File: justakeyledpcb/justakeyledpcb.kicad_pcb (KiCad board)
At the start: 2 copper layers, 84.3 x 43 mm, 16 parts, among them SW1 SW_Push, SW2 SW_Push, SW3 SW_Push, SW4 SW_Push, U1 XIAO-RP2040-DIP

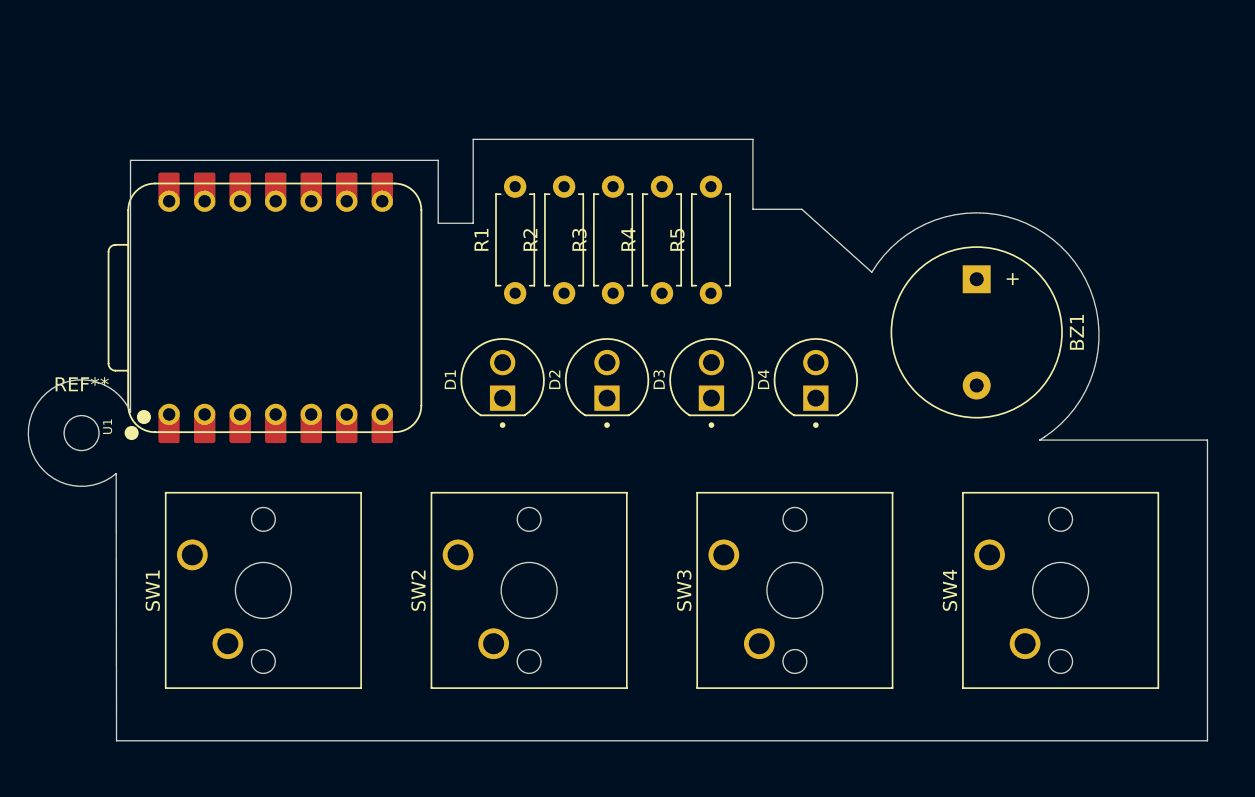
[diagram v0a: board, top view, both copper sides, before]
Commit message: Added the LED's footprints properly
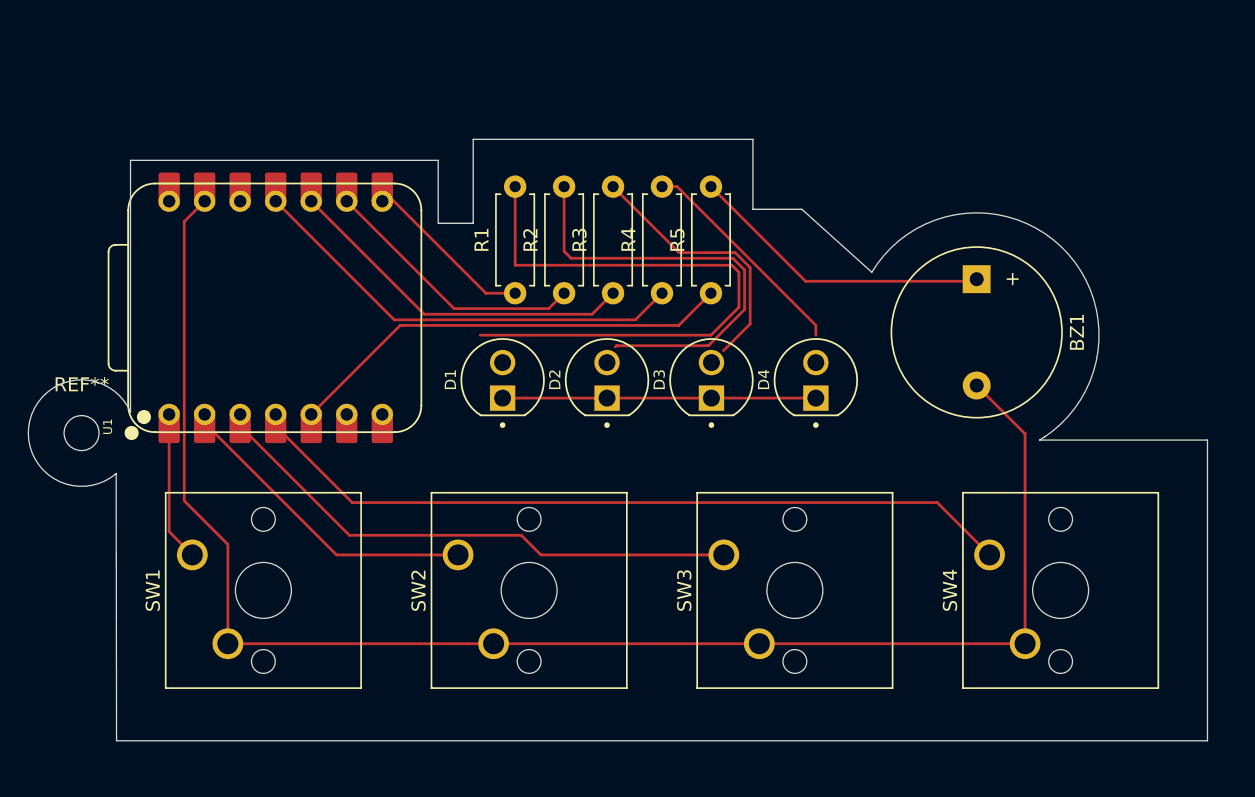
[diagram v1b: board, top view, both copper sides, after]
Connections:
- U1 pad 10: LED 1 -> LED 3
- U1 pad 11: LED 1 -> LED 4
- U1 pad 9: LED 1 -> LED 2
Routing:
- net GND: track 0.00 -> 110.4 mm
- net Button 4: track 0.00 -> 54.9 mm
- net Net-(D1-A): track 0.00 -> 43.7 mm
- net Button 3: track 0.00 -> 38.4 mm
- net Buzzer: track 0.00 -> 33.2 mm
- net LED 4: track 0.00 -> 31.9 mm
- net Net-(D2-A): track 0.00 -> 31.3 mm
- net LED 3: track 0.00 -> 25.5 mm
- net Button 2: track 0.00 -> 22.6 mm
- net (no net): track 0.00 -> 22.4 mm
- net Net-(BZ1-+): track 0.00 -> 21.9 mm
- net LED 2: track 0.00 -> 19.2 mm
- net Net-(D3-A): track 0.00 -> 18.9 mm
- net Net-(D4-A): track 0.00 -> 15.8 mm
- net LED 1: track 0.00 -> 12.6 mm
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
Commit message: FInalised the PCB Schematics and PCB Layout
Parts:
- D1, D2, D3, D4: value LED -> L08R5000Q1; footprint footprints:LEDRD254W57D500H1070 -> e390cee6c564169ed6d49fe7a268946ec8897500_l08r5000q1:LEDRD254W57D500H1070
- moved D1 23.4 mm to (150.5, 58.2)
- moved D4 21.5 mm to (128.0, 58.2)
- moved R1 15.1 mm to (143.0, 49.1)
- moved R5 15.1 mm to (127.0, 49.1)
- moved D2 8.49 mm to (143.0, 58.2)
- moved D3 6.61 mm to (135.5, 58.2)
- moved R4 1.95 mm to (139.0, 49.1)
- moved R3 1.88 mm to (135.0, 49.1)
- moved R2 1.76 mm to (131.0, 49.3)
- moved SW1 0.75 mm to (104.9, 70.5)
- moved SW2 0.75 mm to (123.9, 70.5)
- moved SW3 0.75 mm to (142.9, 70.5)
- moved SW4 0.75 mm to (161.9, 70.5)
- moved BZ1 0.50 mm to (161.5, 50.0)
- moved U1 0.43 mm to (110.9, 51.6)
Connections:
- D1 pad A: (no net) -> Net-(D1-PadA)
- D1 pad C: (no net) -> GND
- D2 pad A: (no net) -> Net-(D2-PadA)
- D2 pad C: (no net) -> GND
- D3 pad A: (no net) -> Net-(D3-PadA)
- D3 pad C: (no net) -> GND
- D4 pad A: (no net) -> Net-(D4-PadA)
- D4 pad C: (no net) -> GND
- R1 pad 1: LED 1 -> Buzzer
- R1 pad 2: Net-(D1-A) -> Net-(BZ1-+)
- R2 pad 2: Net-(D2-A) -> Net-(D3-PadA)
- R3 pad 2: Net-(D3-A) -> Net-(D2-PadA)
- R4 pad 2: Net-(D4-A) -> Net-(D1-PadA)
- R5 pad 1: Buzzer -> LED 1
- R5 pad 2: Net-(BZ1-+) -> Net-(D4-PadA)
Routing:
- net GND: track 110.4 -> 168.5 mm
- net Net-(D1-A): track 43.7 -> 0.00 mm
- net Net-(D4-PadA): track 0.00 -> 35.8 mm
- net Net-(D2-A): track 31.3 -> 0.00 mm
- net Net-(D3-PadA): track 0.00 -> 22.9 mm
- net (no net): track 22.4 -> 0.00 mm
- net Net-(D1-PadA): track 0.00 -> 20.2 mm
- net Net-(D3-A): track 18.9 -> 0.00 mm
- net Net-(D2-PadA): track 0.00 -> 18.8 mm
- net Net-(D4-A): track 15.8 -> 0.00 mm
- net Buzzer: track 33.2 -> 47.2 mm
- net LED 1: track 12.6 -> 10.8 mm
- net Net-(BZ1-+): track 21.9 -> 23.5 mm
- net Button 3: track 38.4 -> 39.9 mm
- net LED 2: track 19.2 -> 18.2 mm
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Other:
- board size 84.3 x 43 mm -> 85.3 x 46 mm

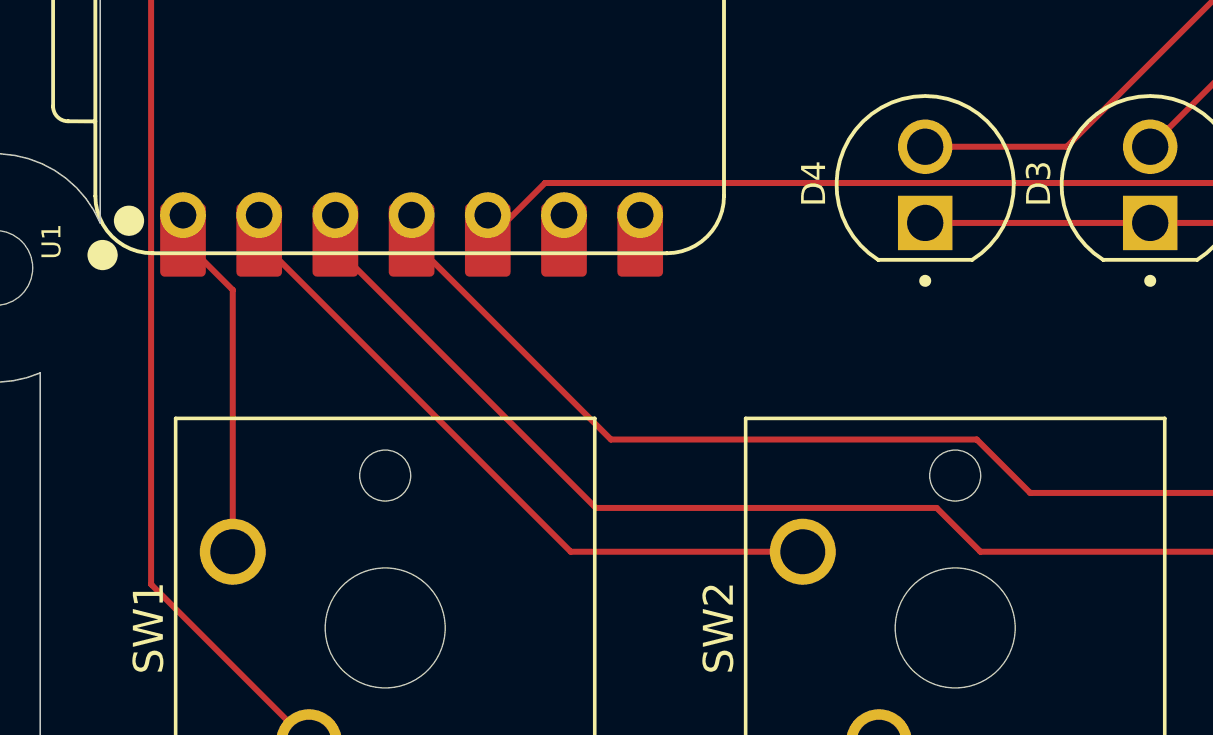
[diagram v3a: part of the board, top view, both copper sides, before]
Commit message: updated the PCB accordingly to the schematic again and saved it
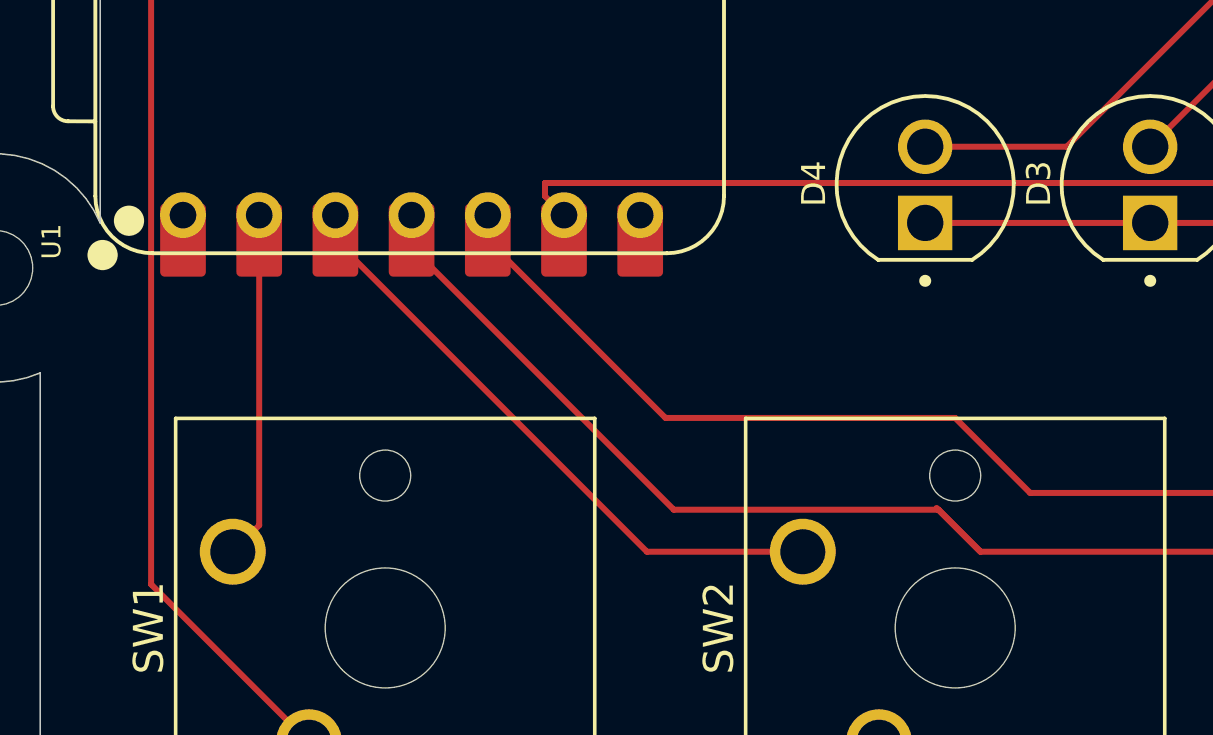
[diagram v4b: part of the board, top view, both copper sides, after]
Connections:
- U1 pad 1: Button 1 -> unconnected-(U1-GPIO26/ADC0/A0-Pad1)
- U1 pad 2: Button 2 -> Button 1
- U1 pad 3: Button 3 -> Button 2
- U1 pad 4: Button 4 -> Button 3
- U1 pad 5: Buzzer -> Button 4
- U1 pad 6: unconnected-(U1-GPIO7/SCL-Pad6) -> Buzzer
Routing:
- net Button 4: track 55.3 -> 52.8 mm
- net Button 2: track 23.3 -> 21.0 mm
- net Buzzer: track 47.2 -> 45.9 mm
- net Button 1: track 11.1 -> 12.4 mm
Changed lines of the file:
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@@
 	(net 15 "Button 4")
 	(net 16 "unconnected-(U1-3V3-Pad12)")
-	(net 17 "unconnected-(U1-GPIO7{slash}SCL-Pad6)")
+	(net 17 "unconnected-(U1-GPIO26{slash}ADC0{slash}A0-Pad1)")
 	(net 18 "unconnected-(U1-VBUS-Pad14)")
 	(net 19 "unconnected-(U1-GPIO0{slash}TX-Pad7)")
@@
 			(layers "F.Cu" "F.Mask")
 			(roundrect_rratio 0.1)
-			(net 12 "Button 1")
+			(net 17 "unconnected-(U1-GPIO26{slash}ADC0{slash}A0-Pad1)")
 			(pinfunction "GPIO26/ADC0/A0")
 			(pintype "passive")
@@
 			(layers "*.Cu" "*.Mask")
 			(remove_unused_layers no)
-			(net 12 "Button 1")
+			(net 17 "unconnected-(U1-GPIO26{slash}ADC0{slash}A0-Pad1)")
 			(pinfunction "GPIO26/ADC0/A0")
 			(pintype "passive")
@@
 			(layers "F.Cu" "F.Mask")
 			(roundrect_rratio 0.1)
-			(net 13 "Button 2")
+			(net 12 "Button 1")
 			(pinfunction "GPIO27/ADC1/A1")
 			(pintype "passive")
@@
 			(layers "*.Cu" "*.Mask")
 			(remove_unused_layers no)
-			(net 13 "Button 2")
+			(net 12 "Button 1")
 			(pinfunction "GPIO27/ADC1/A1")
 			(pintype "passive")
@@
 			(layers "F.Cu" "F.Mask")
 			(roundrect_rratio 0.1)
-			(net 14 "Button 3")
+			(net 13 "Button 2")
 			(pinfunction "GPIO28/ADC2/A2")
 			(pintype "passive")
@@
 			(layers "*.Cu" "*.Mask")
 			(remove_unused_layers no)
-			(net 14 "Button 3")
+			(net 13 "Button 2")
 			(pinfunction "GPIO28/ADC2/A2")
 			(pintype "passive")
@@
 			(layers "F.Cu" "F.Mask")
 			(roundrect_rratio 0.1)
-			(net 15 "Button 4")
+			(net 14 "Button 3")
 			(pinfunction "GPIO29/ADC3/A3")
 			(pintype "passive")
@@
 			(layers "*.Cu" "*.Mask")
 			(remove_unused_layers no)
-			(net 15 "Button 4")
+			(net 14 "Button 3")
 			(pinfunction "GPIO29/ADC3/A3")
 			(pintype "passive")
@@
 			(layers "F.Cu" "F.Mask")
 			(roundrect_rratio 0.1)
-			(net 11 "Buzzer")
+			(net 15 "Button 4")
 			(pinfunction "GPIO6/SDA")
 			(pintype "passive")
@@
 			(layers "*.Cu" "*.Mask")
 			(remove_unused_layers no)
-			(net 11 "Buzzer")
+			(net 15 "Button 4")
 			(pinfunction "GPIO6/SDA")
 			(pintype "passive")
@@
 			(layers "F.Cu" "F.Mask")
 			(roundrect_rratio 0.1)
-			(net 17 "unconnected-(U1-GPIO7{slash}SCL-Pad6)")
+			(net 11 "Buzzer")
 			(pinfunction "GPIO7/SCL")
 			(pintype "passive")
@@
 			(layers "*.Cu" "*.Mask")
 			(remove_unused_layers no)
-			(net 17 "unconnected-(U1-GPIO7{slash}SCL-Pad6)")
+			(net 11 "Buzzer")
 			(pinfunction "GPIO7/SCL")
 			(pintype "passive")
@@
 	)
 	(segment
+		(start 115.96 59.24)
+		(end 115.3265 58.6065)
+		(width 0.2)
+		(layer "F.Cu")
+		(net 11)
+	)
+	(segment
 		(start 115.3265 58.1685)
 		(end 147.8315 58.1685)
@@
 	)
 	(segment
-		(start 113.42 60.075)
+		(start 115.3265 58.6065)
 		(end 115.3265 58.1685)
 		(width 0.2)
@@
 	)
 	(segment
-		(start 104.92 61.735)
-		(end 103.26 60.075)
+		(start 105.8 69.58)
+		(end 104.92 70.46)
+		(width 0.2)
+		(layer "F.Cu")
+		(net 12)
+	)
+	(segment
+		(start 105.8 60.075)
+		(end 105.8 59.24)
 		(width 0.2)
 		(layer "F.Cu")
@@
 	)
 	(segment
-		(start 104.92 70.46)
-		(end 104.92 61.735)
+		(start 105.8 59.24)
+		(end 105.8 69.58)
 		(width 0.2)
 		(layer "F.Cu")
@@
 	)
 	(segment
-		(start 123.92 70.46)
-		(end 116.185 70.46)
+		(start 108.34 59.24)
+		(end 108.34 60.31763)
 		(width 0.2)
 		(layer "F.Cu")
@@
 	)
 	(segment
-		(start 105.8 60.075)
-		(end 105.8 59.24)
+		(start 108.34 60.075)
+		(end 118.725 70.46)
 		(width 0.2)
 		(layer "F.Cu")
@@
 	)
 	(segment
-		(start 116.185 70.46)
-		(end 105.8 60.075)
+		(start 118.725 70.46)
+		(end 123.92 70.46)
 		(width 0.2)
 		(layer "F.Cu")
@@
 	)
 	(segment
-		(start 108.34 59.24)
-		(end 108.34 60.31763)
+		(start 119.62137 69.059)
+		(end 128.44053 69.059)
 		(width 0.2)
 		(layer "F.Cu")
@@
 	)
 	(segment
-		(start 108.34 60.31763)
-		(end 117.02237 69)
+		(start 128.44053 69.059)
+		(end 129.84153 70.46)
 		(width 0.2)
 		(layer "F.Cu")
@@
 	)
 	(segment
-		(start 117.02237 69)
-		(end 128.38153 69)
+		(start 110.88 59.24)
+		(end 110.88 60.31763)
 		(width 0.2)
 		(layer "F.Cu")
@@
 	)
 	(segment
+		(start 110.88 60.31763)
+		(end 119.62137 69.059)
+		(width 0.2)
+		(layer "F.Cu")
+		(net 14)
+	)
+	(segment
 		(start 128.38153 69)
 		(end 129.84153 70.46)
@@
 	)
 	(segment
-		(start 131.5 68.5)
-		(end 146.5 68.5)
+		(start 113.42 60.075)
+		(end 119.345 66)
 		(width 0.2)
 		(layer "F.Cu")
@@
 	)
 	(segment
-		(start 146.5 68.5)
-		(end 148.46 70.46)
+		(start 119.345 66)
+		(end 129 66)
 		(width 0.2)
 		(layer "F.Cu")
@@
 	)
 	(segment
-		(start 110.88 60.075)
-		(end 117.524 66.719)
+		(start 148.46 70.46)
+		(end 161.92 70.46)
 		(width 0.2)
 		(layer "F.Cu")
@@
 	)
 	(segment
-		(start 129.719 66.719)
+		(start 129 66)
 		(end 131.5 68.5)
 		(width 0.2)
@@
 	)
 	(segment
-		(start 148.46 70.46)
-		(end 161.92 70.46)
+		(start 131.5 68.5)
+		(end 146.5 68.5)
 		(width 0.2)
 		(layer "F.Cu")
@@
 	)
 	(segment
-		(start 117.524 66.719)
-		(end 129.719 66.719)
+		(start 146.5 68.5)
+		(end 148.46 70.46)
 		(width 0.2)
 		(layer "F.Cu")

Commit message: added the place for an external power source in the PCB schem and updated the PCB design
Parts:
- added BT1: Battery, TestPoint:TestPoint_2Pads_Pitch2.54mm_Drill0.8mm, F.Cu at (100.5, 82.0)
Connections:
- U1 pad 14: unconnected-(U1-VBUS-Pad14) -> VCC
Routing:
- net VCC: track 0.00 -> 39.2 mm
- net GND: track 168.5 -> 203.2 mm
